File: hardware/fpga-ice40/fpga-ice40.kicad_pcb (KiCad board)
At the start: 4 copper layers, 53.3 x 48.6 mm, 87 parts, among them J1 MicroSD_Molex_1040310811, J2 Conn_01x03, J4 Conn_02x20_Odd_Even, J5 USB_B_Micro, J6 Conn_02x05_Odd_Even, J7 Conn_02x05_Odd_Even, Q1 2N7002H, U1 iCE40HX4K-TQ144, U2 IS42S16320F-6TL, U3 W25Q32JVSS, U4 W25Q32JVSS, U5 S25FL256SAGMFI01, U6 S25FL256SAGMFI01, U7 FT245RL, U8 AZ1117-1.2, U9 AZ1117-1.2, X1 ECS-2520MV-xxx-xx

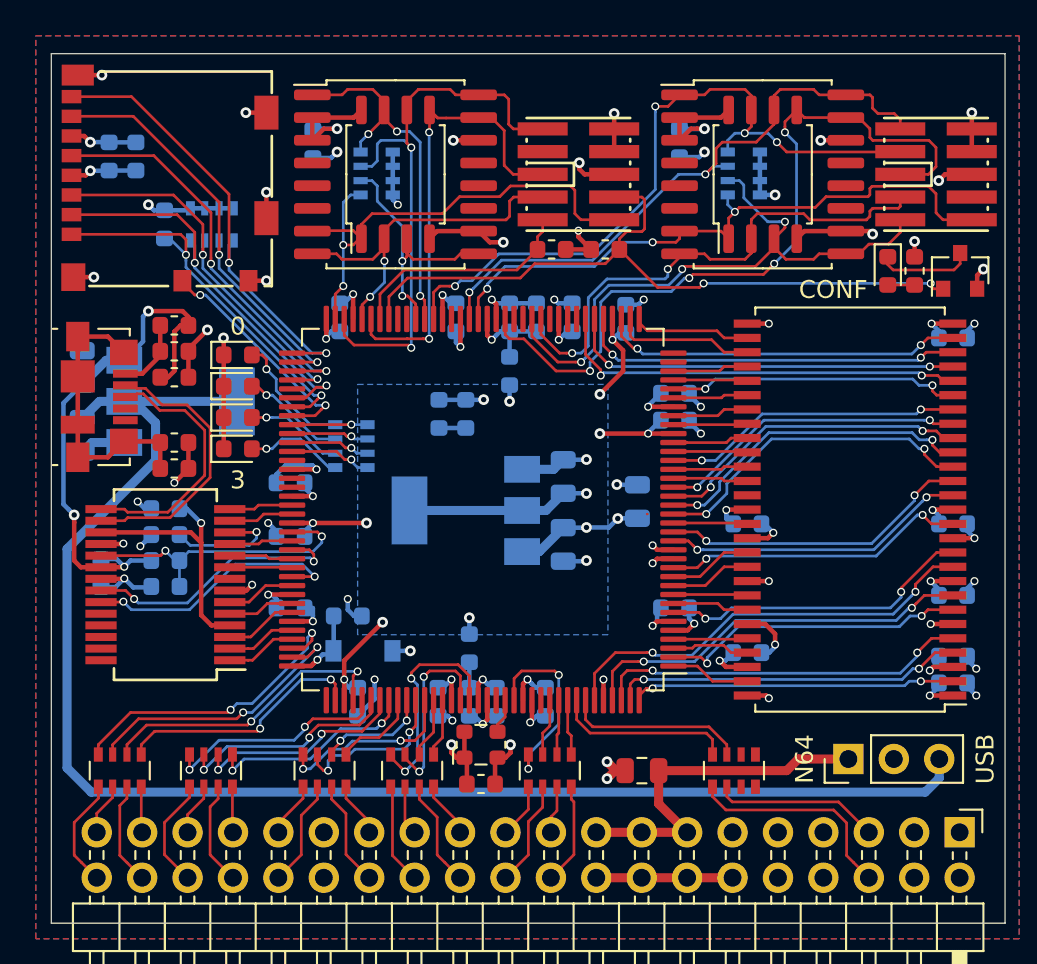
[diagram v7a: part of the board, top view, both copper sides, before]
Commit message: Completed first pass routing with DRC checks passing
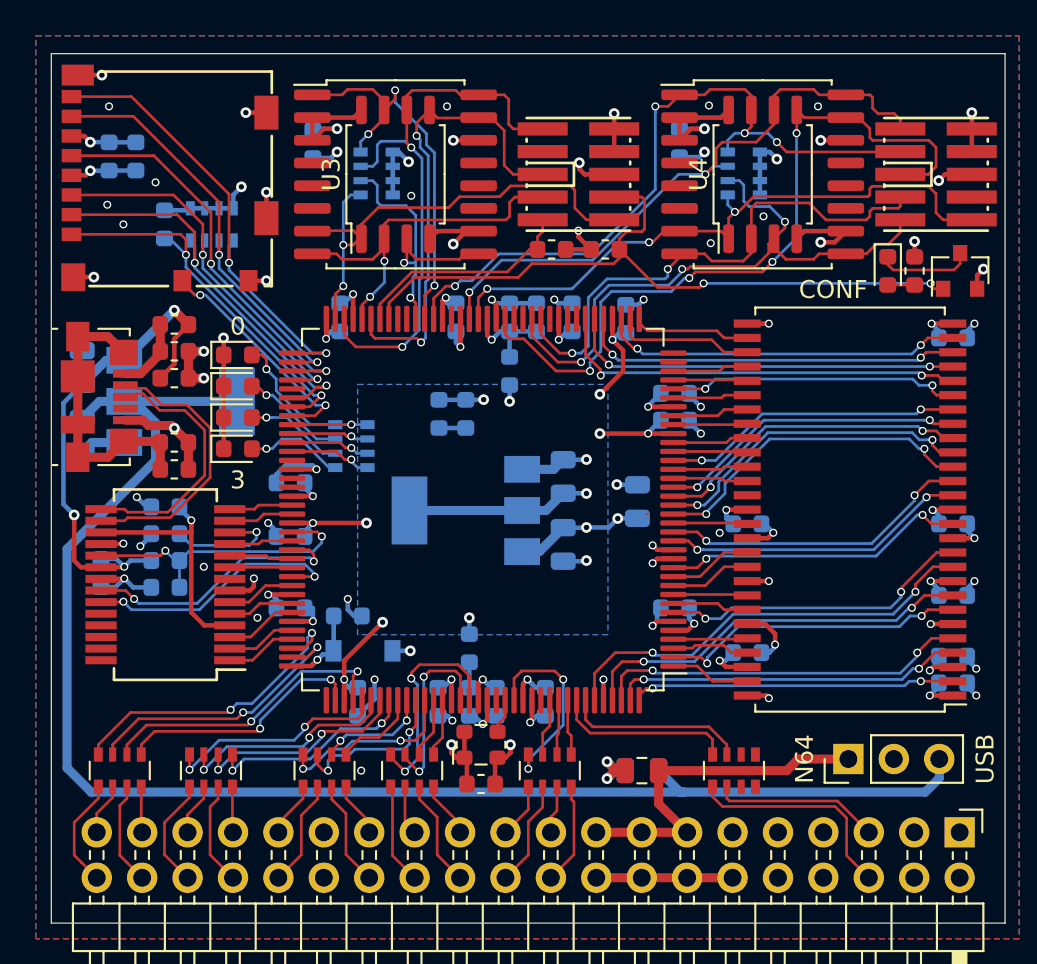
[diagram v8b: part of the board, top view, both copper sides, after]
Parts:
- added C44: 10u, Capacitor_SMD:C_0805_2012Metric, B.Cu at (168.9, 109.6)
- U3, U4: footprint Package_SO:SOIC-8_5.275x5.275mm_P1.27mm -> local_hacks:SOIC-8_5.275x5.275mm_P1.27mm__No_CrtYd
- moved C33 0.10 mm to (142.2, 94.8)
- moved C41 0.05 mm to (142.8, 87.7)
- moved R9 0.05 mm to (142.2, 96.3)
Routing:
- net GND: track 117.1 -> 123.3 mm, vias 55 -> 70
- net CONFIG_IO3: track 21.3 -> 23.6 mm
- net USB_3V3: track 83.4 -> 85.3 mm
- net CONFIG_IO2: track 16.0 -> 17.5 mm
- net USB_5V: track 29.8 -> 28.3 mm
- net P3V3: track 92.0 -> 93.0 mm
- net FLASH_MISO|IO1: track 29.9 -> 30.8 mm
- net /USB_VIO: track 14.4 -> 13.7 mm
- net FLASH_MOSI|IO0: track 43.0 -> 42.4 mm
- net CONFIG_MOSI|IO0: track 27.7 -> 28.2 mm
